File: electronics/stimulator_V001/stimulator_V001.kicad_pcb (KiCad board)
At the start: 2 copper layers, 2 parts

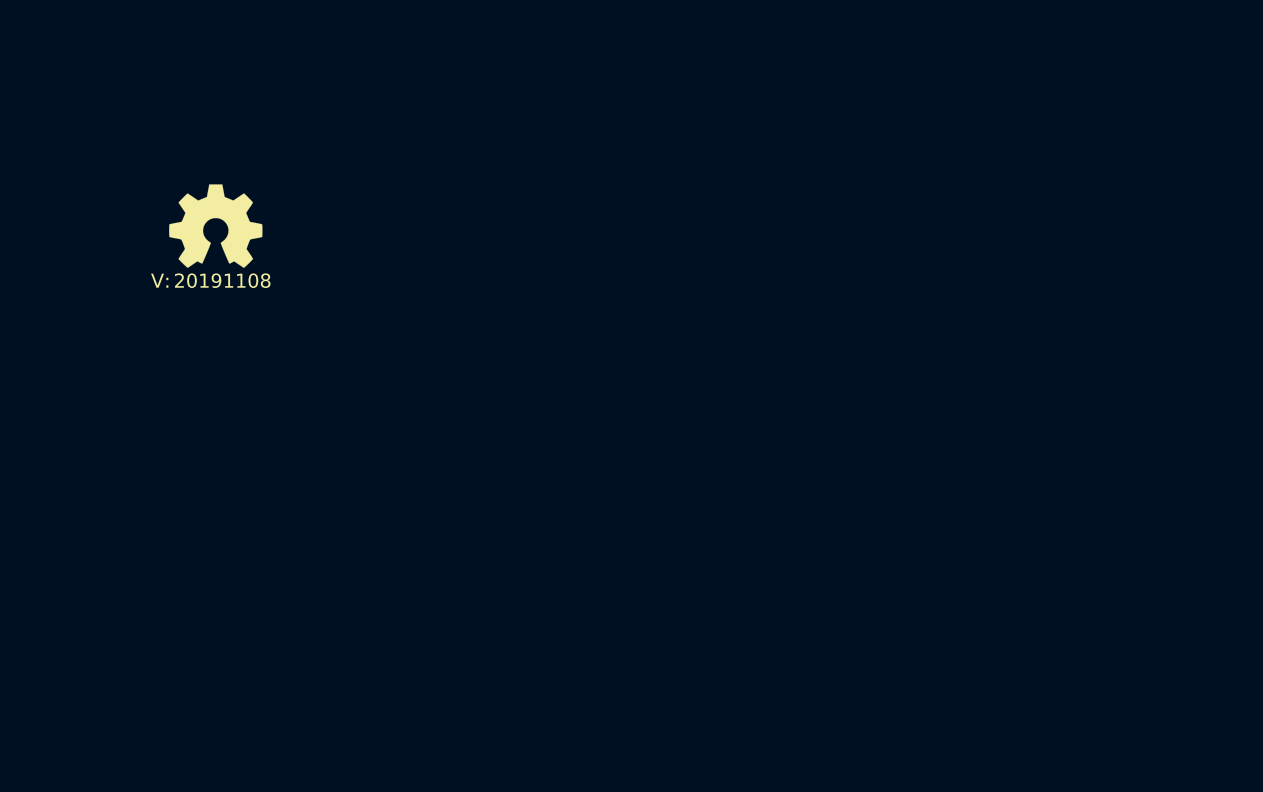
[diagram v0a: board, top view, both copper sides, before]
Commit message: started PCB layout, DRC passes
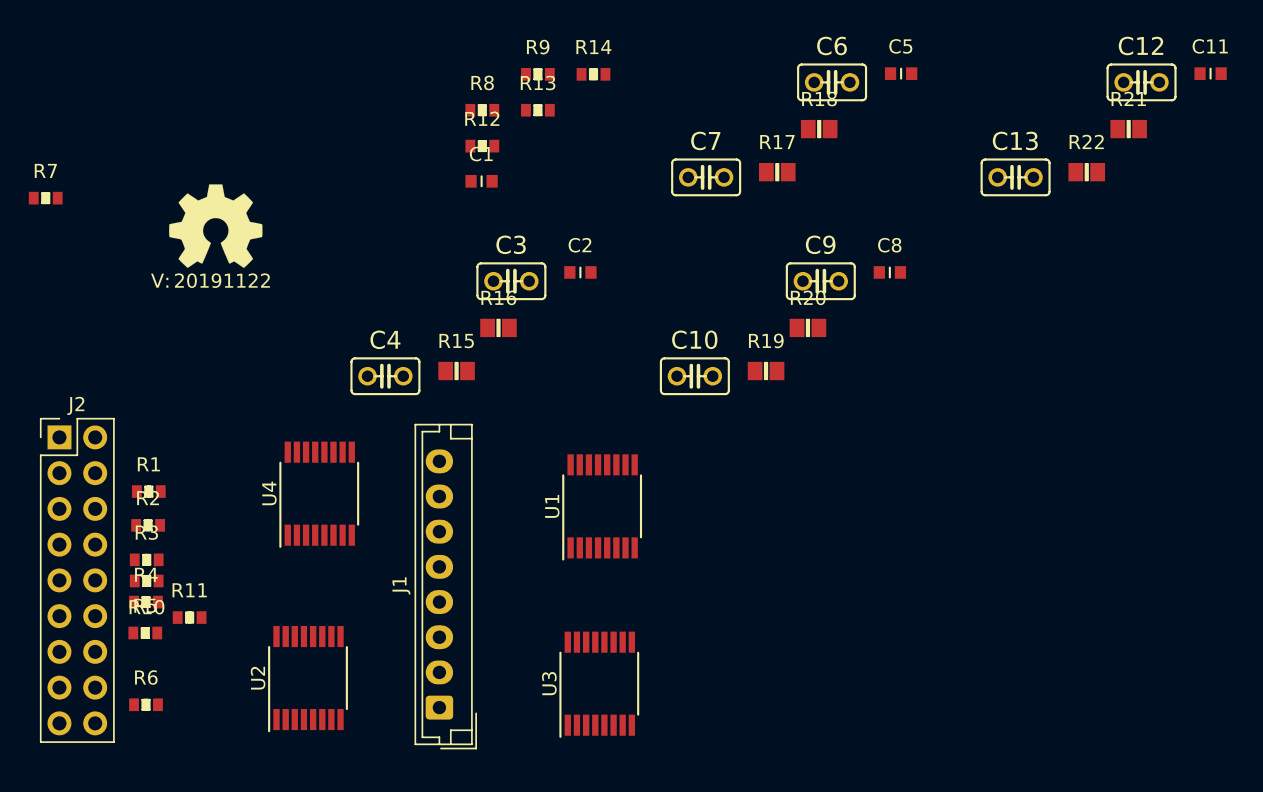
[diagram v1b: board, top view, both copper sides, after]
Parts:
- added C1: 10u, SquantorRcl:C_0603, F.Cu at (166.9, 97.8)
- added C10: 100n, SquantorRcl:C025-025X050, F.Cu at (182.1, 111.7)
- added C11: 10u, SquantorRcl:C_0603, F.Cu at (218.7, 90.2)
- added C12: 100n, SquantorRcl:C025-025X050, F.Cu at (213.8, 90.8)
- added C13: 100n, SquantorRcl:C025-025X050, F.Cu at (204.8, 97.5)
- added C2: 10u, SquantorRcl:C_0603, F.Cu at (173.9, 104.3)
- added C3: 100n, SquantorRcl:C025-025X050, F.Cu at (169.0, 104.9)
- added C4: 100n, SquantorRcl:C025-025X050, F.Cu at (160.1, 111.7)
- added C5: 10u, SquantorRcl:C_0603, F.Cu at (196.7, 90.2)
- added C6: 100n, SquantorRcl:C025-025X050, F.Cu at (191.8, 90.8)
- added C7: 100n, SquantorRcl:C025-025X050, F.Cu at (182.9, 97.5)
- added C8: 10u, SquantorRcl:C_0603, F.Cu at (195.9, 104.3)
- added C9: 100n, SquantorRcl:C025-025X050, F.Cu at (191.0, 104.9)
- added J1: Conn_01x08, Connector_JST:JST_EH_B8B-EH-A_1x08_P2.50mm_Vertical, F.Cu at (163.9, 135.2)
- added J2: Conn_02x08_Odd_Even, Connector_PinHeader_2.54mm:PinHeader_2x09_P2.54mm_Vertical, F.Cu at (136.9, 116.0)
- added R1: 100, SquantorRcl:R_0603_hand, F.Cu at (143.2, 119.8)
- added R10: 100, SquantorRcl:R_0603_hand, F.Cu at (143.1, 126.2)
- added R11: 100, SquantorRcl:R_0603_hand, F.Cu at (146.2, 128.8)
- added R12: 100, SquantorRcl:R_0603_hand, F.Cu at (166.9, 95.3)
- added R13: 100, SquantorRcl:R_0603_hand, F.Cu at (170.9, 92.8)
- added R14: 100, SquantorRcl:R_0603_hand, F.Cu at (174.8, 90.2)
- added R15: 10K, SquantorRcl:R_0805+0603, F.Cu at (165.1, 111.3)
- added R16: 10K, SquantorRcl:R_0805+0603, F.Cu at (168.1, 108.2)
- added R17: 10K, SquantorRcl:R_0805+0603, F.Cu at (187.9, 97.2)
- added R18: 10K, SquantorRcl:R_0805+0603, F.Cu at (190.9, 94.1)
- added R19: 10K, SquantorRcl:R_0805+0603, F.Cu at (187.1, 111.3)
- added R2: 100, SquantorRcl:R_0603_hand, F.Cu at (143.2, 122.2)
- added R20: 10K, SquantorRcl:R_0805+0603, F.Cu at (190.1, 108.2)
- added R21: 10K, SquantorRcl:R_0805+0603, F.Cu at (212.9, 94.1)
- added R22: 10K, SquantorRcl:R_0805+0603, F.Cu at (209.9, 97.2)
- added R3: 100, SquantorRcl:R_0603_hand, F.Cu at (143.1, 124.7)
- added R4: 100, SquantorRcl:R_0603_hand, F.Cu at (143.1, 127.7)
- added R5: 100, SquantorRcl:R_0603_hand, F.Cu at (143.0, 129.9)
- added R6: 100, SquantorRcl:R_0603_hand, F.Cu at (143.1, 135.0)
- added R7: 4.7K, SquantorRcl:R_0603_hand, F.Cu at (135.9, 99.0)
- added R8: 100, SquantorRcl:R_0603_hand, F.Cu at (166.9, 92.8)
- added R9: 100, SquantorRcl:R_0603_hand, F.Cu at (170.9, 90.2)
- added U1: 74XX4052, Package_SO:TSSOP-16_4.4x5mm_P0.65mm, F.Cu at (175.5, 120.9)
- added U2: 74XX4052, Package_SO:TSSOP-16_4.4x5mm_P0.65mm, F.Cu at (154.6, 133.1)
- added U3: 74XX4052, Package_SO:TSSOP-16_4.4x5mm_P0.65mm, F.Cu at (175.3, 133.5)
- added U4: 74XX4052, Package_SO:TSSOP-16_4.4x5mm_P0.65mm, F.Cu at (155.4, 120.0)
- N2: value 20191108 -> 20191122

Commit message: further placement
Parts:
- R1, R10, R11, R12, R13, R14, R2, R3, R4, R5, R6, R7, R8, R9: footprint SquantorRcl:R_0603_hand -> SquantorRcl:R_0402_hand
- moved C11 80.2 mm to (143.2, 117.1), turned to 90 degrees
- moved C12 69.6 mm to (150.5, 119.6), turned to 90 degrees
- moved C6 58.9 mm to (150.3, 132.6), turned to 90 degrees
- moved R14 55.9 mm to (143.2, 136.3), turned to 180 degrees
- moved R21 54.1 mm to (166.2, 121.5), turned to 90 degrees
- moved R13 49.5 mm to (143.2, 133.8), turned to 180 degrees
- moved C13 49.4 mm to (160.9, 120.1), turned to 270 degrees
- moved R22 48.6 mm to (166.2, 118.4), turned to 270 degrees
- moved R9 43.4 mm to (143.2, 123.6), turned to 180 degrees
- moved R12 43.0 mm to (143.2, 131.2), turned to 180 degrees
- moved C8 41.9 mm to (155.1, 113.7)
- moved C7 41.5 mm to (160.2, 132.3), turned to 90 degrees
- moved R18 41.0 mm to (166.2, 126.8), turned to 90 degrees
- moved R17 39.4 mm to (166.2, 130.0), turned to 90 degrees
- moved R8 37.0 mm to (143.2, 121.1), turned to 180 degrees
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
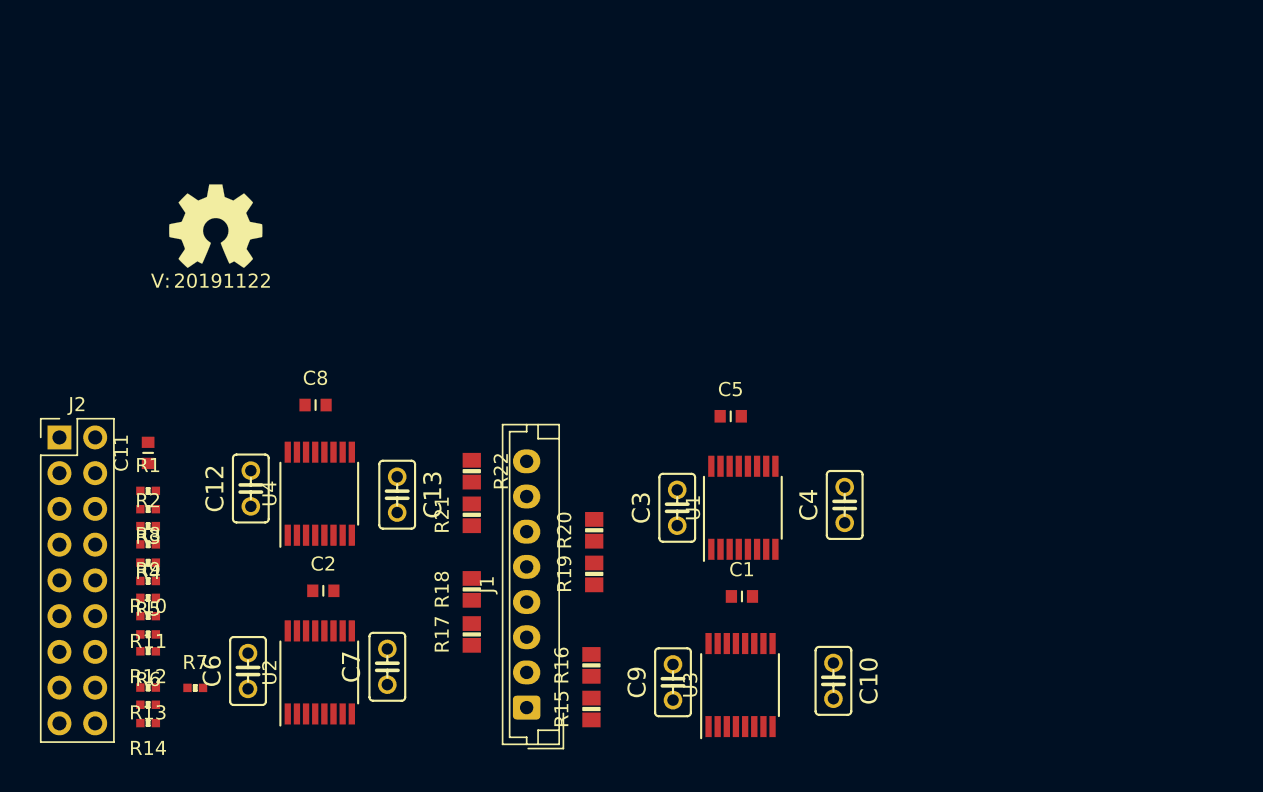
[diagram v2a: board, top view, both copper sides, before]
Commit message: more placement iterations
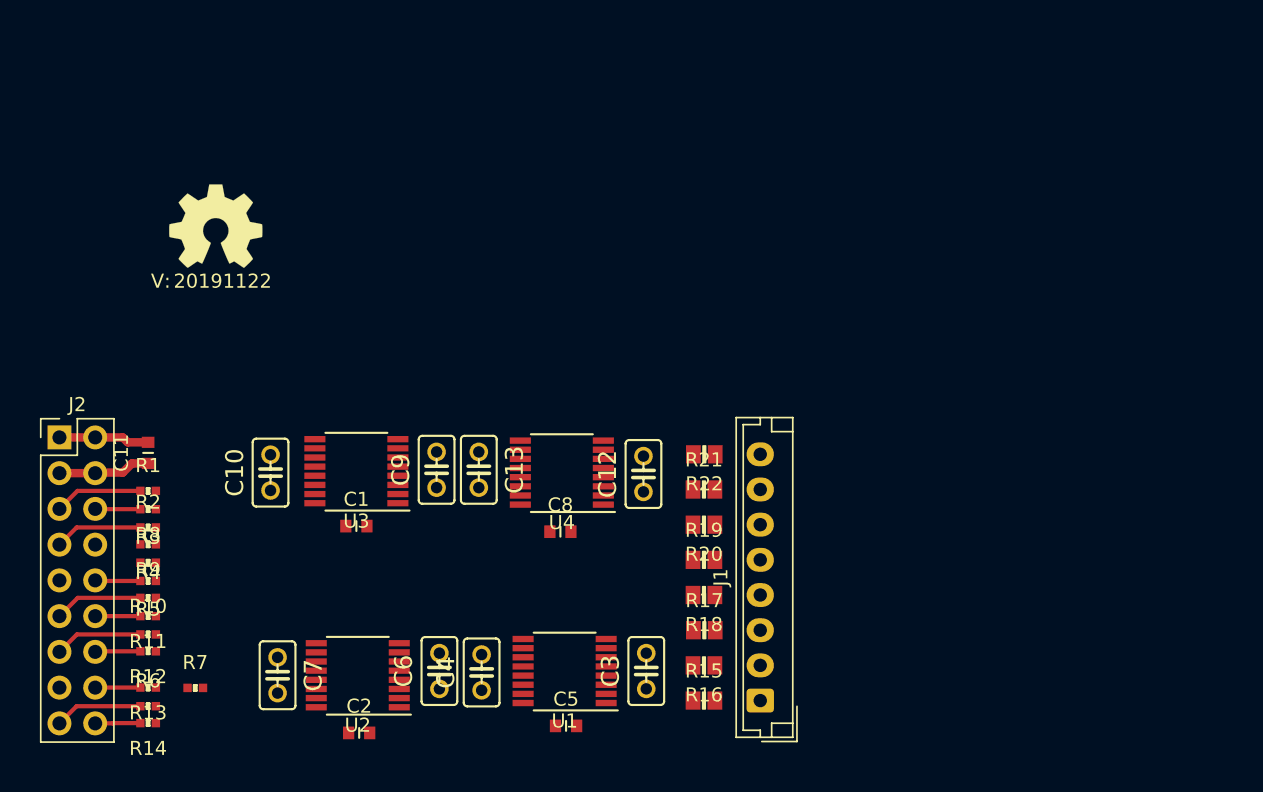
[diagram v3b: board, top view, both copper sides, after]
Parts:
- moved C10 42.7 mm to (151.9, 118.5), turned to 90 degrees
- moved U3 31.2 mm to (158.0, 118.4), turned to 180 degrees
- moved C4 28.4 mm to (166.9, 132.7)
- moved C12 27.9 mm to (178.4, 118.6)
- moved C1 27.9 mm to (158.0, 122.3)
- moved C5 24.9 mm to (172.9, 136.5)
- moved C9 22.6 mm to (163.7, 118.3)
- moved C8 19.6 mm to (172.5, 122.7)
- moved U4 17.3 mm to (172.6, 118.5), turned to 180 degrees
- moved U1 17.2 mm to (172.8, 132.6), turned to 180 degrees
- moved J1 16.6 mm to (186.7, 134.7)
- moved R21 16.6 mm to (182.7, 119.7), turned to 0 degrees
- moved R22 16.6 mm to (182.7, 117.2), turned to 180 degrees
- moved R17 16.5 mm to (182.7, 129.7), turned to 0 degrees
- moved R18 16.5 mm to (182.7, 127.2), turned to 180 degrees
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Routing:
- net /VDD: track 0.00 -> 6.59 mm
- net /VSS: track 0.00 -> 6.44 mm
- net Net-(J2-Pad11): track 0.00 -> 6.29 mm
- net Net-(J2-Pad5): track 0.00 -> 6.28 mm
- net Net-(J2-Pad13): track 0.00 -> 6.26 mm
- net Net-(J2-Pad7): track 0.00 -> 6.26 mm
- net Net-(J2-Pad17): track 0.00 -> 6.26 mm
- net Net-(J2-Pad14): track 0.00 -> 3.23 mm
- net Net-(J2-Pad10): track 0.00 -> 3.23 mm
- net Net-(J2-Pad6): track 0.00 -> 3.22 mm
- net Net-(J2-Pad18): track 0.00 -> 3.22 mm
- net Net-(J2-Pad16): track 0.00 -> 3.21 mm
- net Net-(J2-Pad12): track 0.00 -> 3.21 mm

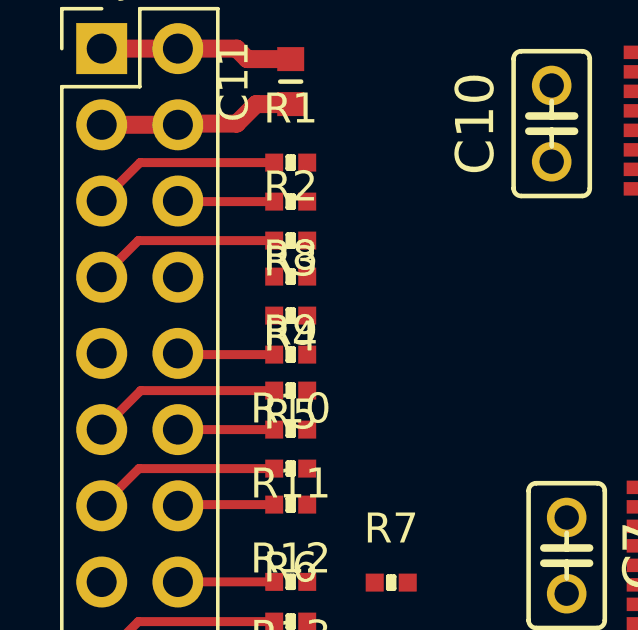
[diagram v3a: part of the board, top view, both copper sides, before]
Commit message: more placement optimizations
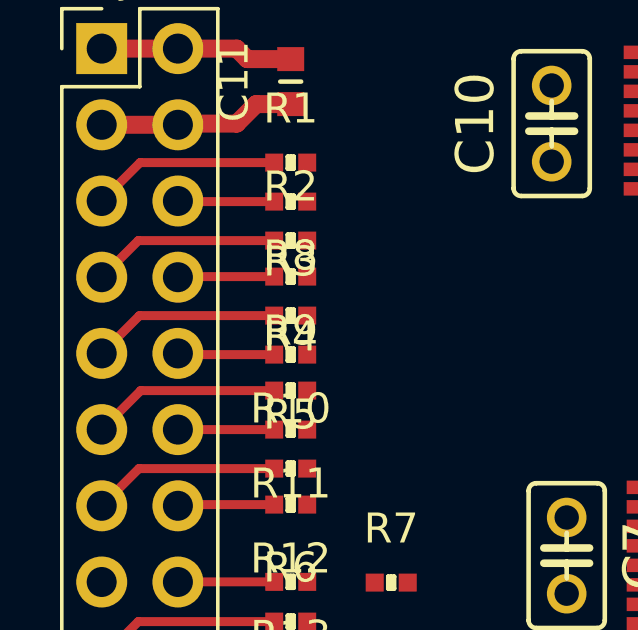
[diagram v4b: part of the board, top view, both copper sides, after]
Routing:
- net Net-(J2-Pad9): track 0.00 -> 6.27 mm
- net Net-(J2-Pad8): track 0.00 -> 3.22 mm
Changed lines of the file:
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@@
     (thickness 1.6)
     (drawings 0)
-    (tracks 31)
+    (tracks 35)
     (zones 0)
     (modules 43)
@@
   )
   (setup
-    (last_trace_width 0.6)
+    (last_trace_width 0.3)
     (user_trace_width 0.15)
     (user_trace_width 0.2)
@@
   (segment (start 138.12 122.4) (end 142.65 122.4) (width 0.3) (layer F.Cu) (net 14))
   (segment (start 136.9 123.62) (end 138.12 122.4) (width 0.3) (layer F.Cu) (net 14))
+  (segment (start 138.16 124.9) (end 142.65 124.9) (width 0.3) (layer F.Cu) (net 16))
+  (segment (start 136.9 126.16) (end 138.16 124.9) (width 0.3) (layer F.Cu) (net 16))
   (segment (start 136.9 128.7) (end 138.2 127.4) (width 0.3) (layer F.Cu) (net 18))
   (segment (start 138.2 127.4) (end 142.65 127.4) (width 0.3) (layer F.Cu) (net 18))
@@
   (segment (start 139.46 121.1) (end 142.65 121.1) (width 0.3) (layer F.Cu) (net 24))
   (segment (start 139.44 121.08) (end 139.46 121.1) (width 0.3) (layer F.Cu) (net 24))
+  (segment (start 139.46 123.6) (end 142.65 123.6) (width 0.3) (layer F.Cu) (net 26))
+  (segment (start 139.44 123.62) (end 139.46 123.6) (width 0.3) (layer F.Cu) (net 26))
   (segment (start 139.48 126.2) (end 142.65 126.2) (width 0.3) (layer F.Cu) (net 28))
   (segment (start 139.44 126.16) (end 139.48 126.2) (width 0.3) (layer F.Cu) (net 28))
